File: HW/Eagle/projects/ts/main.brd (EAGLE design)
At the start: 85 x 45 mm, 29 parts, among them IC1 4050D, U1 ATMEGA328P-PU, U2 LM2576T, U3 HT7533

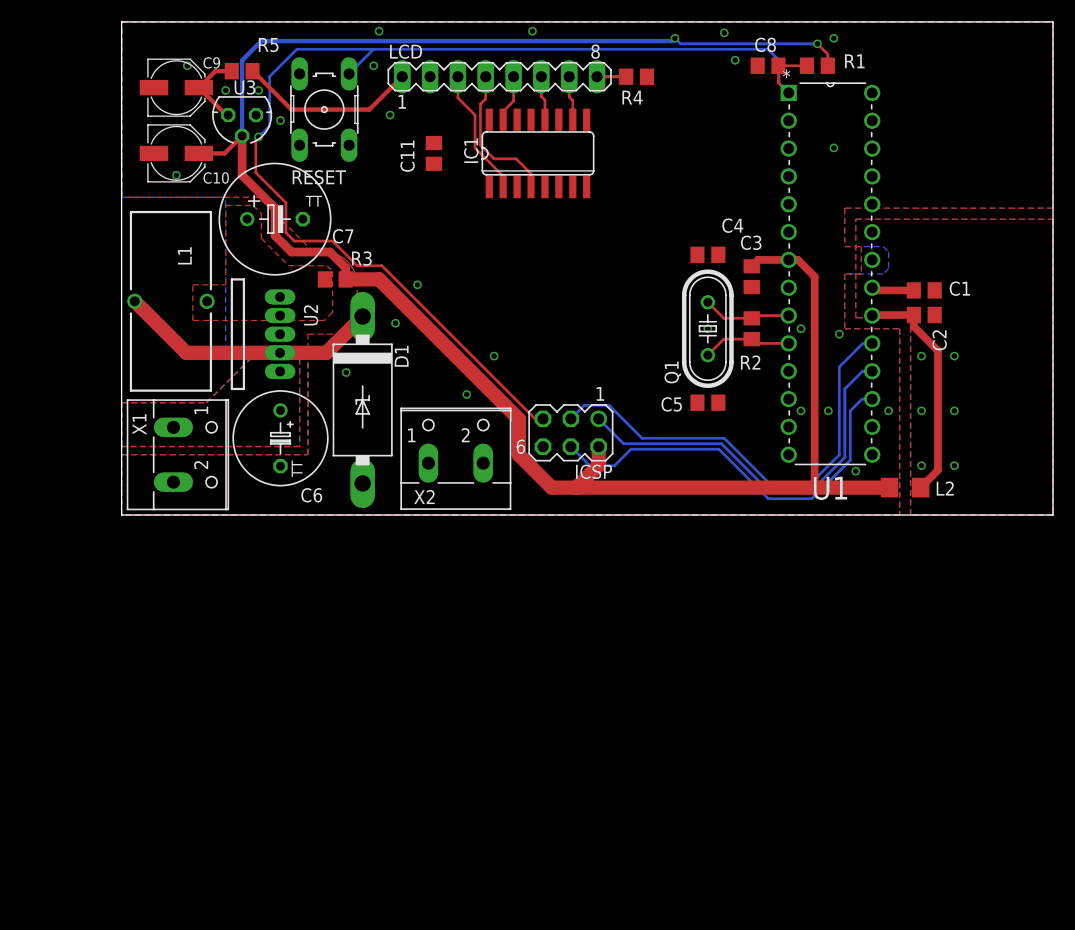
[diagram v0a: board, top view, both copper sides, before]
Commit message: Commit before changing to digital temperature sensor
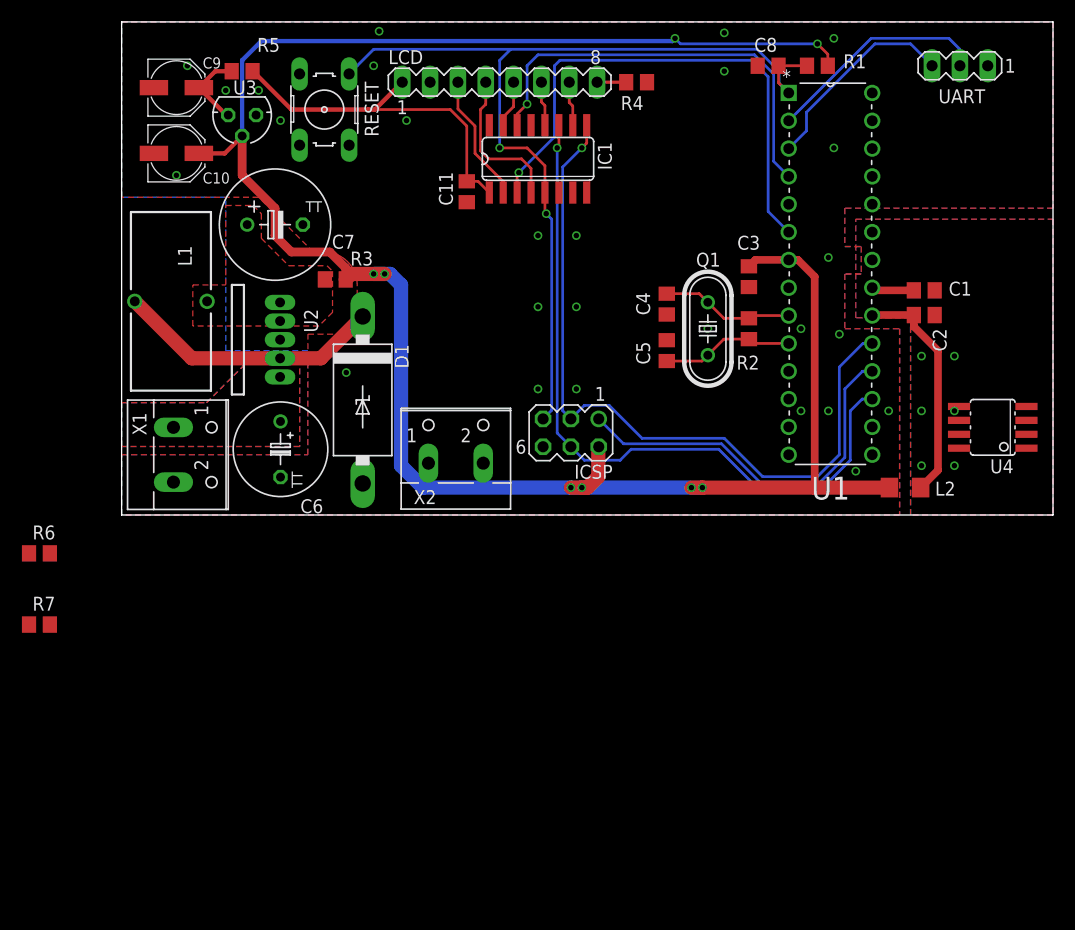
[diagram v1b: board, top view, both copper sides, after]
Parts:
- added R6, R7: 4.7k, rcl:R0805
- added U4: LM75, misc:SOIC8
- added UART: (no value), con-lstb:MA03-1
- moved C5 6.05 mm to (49.8, 15.0), turned to 270 degrees
- moved C4 5.86 mm to (49.8, 19.2), turned to 90 degrees
- moved C11 4.61 mm to (31.5, 29.5), turned to 90 degrees
- moved C6 1.00 mm to (14.5, 6.00)
- moved C7 0.50 mm to (14.0, 26.5)
- moved IC1 0.50 mm to (38.0, 32.5)
- moved LCD 0.50 mm to (34.5, 39.5)
- moved R4 0.50 mm to (47.0, 39.5)
- moved U2 0.50 mm to (12.5, 16.0)
- moved C3 0.25 mm to (57.2, 21.8)
- moved R2 0.25 mm to (57.2, 17.0)
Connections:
- new net LCD_DC_5V: IC1.3, U1.6
- new net LCD_LED_5V: U1.5
- new net LCD_SCE_5V: IC1.14, U1.4
- new net SCL: R6.1, U1.28, U4.2
- new net SDA: R7.1, U1.27, U4.1
- net GND: now also U4.4, UART.1
- net NRST: now also IC1.5
- net RXD: now also UART.2
- net TXD: now also UART.3
- net VCC: now also R6.2, R7.2, U4.8
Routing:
- net LCD_DC_5V: track 0.00 -> 48.3 mm, vias 0 -> 1
- net LCD_SCE_5V: track 0.00 -> 39.4 mm, vias 0 -> 1
- net MOSI: track 37.1 -> 65.8 mm, vias 0 -> 1
- net SCK: track 41.3 -> 68.4 mm, vias 0 -> 1
- net RXD: track 0.00 -> 20.6 mm
- net NRST: track 106.3 -> 86.7 mm, vias 1 -> 2
- net TXD: track 0.00 -> 18.9 mm
- net +3V3: track 16.4 -> 33.3 mm
- net VCC: track 176.4 -> 187.9 mm, vias 2 -> 8
- net N$4: track 8.09 -> 12.1 mm
- net N$3: track 8.15 -> 12.1 mm
- net MISO: track 36.0 -> 35.2 mm
- net LCD_RST: track 13.4 -> 13.9 mm

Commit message: Big Update
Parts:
- removed L2: 10uH, misc:L1206
- added C12: 100nF, rcl:C0805
- added D2, D3: (no value), diode:MINIMELF
- added KEYPAD: (no value), con-lstb:MA07-1
- added LED: (no value), jumper:JP1
- added R10, R11: 10k, rcl:R0805
- added R8: 4.7k, rcl:R0805
- added R9: 330R, rcl:R0805
- added T1, T2: IRLML2502, misc:SOT-23
- moved R6 87.2 mm to (77.0, 18.0), turned to 90 degrees
- moved R7 85.7 mm to (73.5, 18.0), turned to 90 degrees
- moved UART 26.5 mm to (50.5, 36.0), turned to 270 degrees
- moved R4 7.43 mm to (44.5, 32.5), turned to 90 degrees
- moved U4 6.10 mm to (74.5, 11.5)
- moved C4 5.50 mm to (44.2, 19.2)
- moved C5 5.50 mm to (44.2, 15.0)
- moved C8 5.02 mm to (54.0, 41.5)
- moved R1 5.02 mm to (58.5, 41.5)
- moved C1 5.00 mm to (68.2, 20.5)
- moved C2 5.00 mm to (68.2, 18.2)
- moved Q1 5.00 mm to (48.5, 17.0)
- moved U1 5.00 mm to (63.5, 5.50)
- moved C3 4.75 mm to (52.5, 21.8)
- moved R2 4.75 mm to (52.5, 17.0)
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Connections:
- removed net AVCC: C2.2, L2.1, U1.20
- new net KEYPAD_C0: KEYPAD.1, U1.13
- new net KEYPAD_C1: KEYPAD.2, U1.12
- new net KEYPAD_C2: KEYPAD.3, U1.11
- new net KEYPAD_R0: KEYPAD.4, U1.23
- new net KEYPAD_R1: KEYPAD.5, U1.24
- new net KEYPAD_R2: KEYPAD.6, U1.25
- new net KEYPAD_R3: KEYPAD.7, U1.26
- new net LED: LED.2, U1.16
- new net N$10: D2.A, T1.3, X2.1
- new net N$11: D3.A, T2.3, X2.2
- new net N$5: R8.1, U4.5, U4.6, U4.7
- new net N$6: LED.1, R9.2
- new net OUT1: R10.2, T1.1, U1.14
- new net OUT2: R11.2, T2.1, U1.15
- net +12V: now also D2.C, D3.C
- net GND: now also C12.1, R10.1, R11.1, T1.2, T2.2
- net VCC: now also C12.2, C2.2, R8.2, R9.1, U1.20; no longer L2.2
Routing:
- net SDA: track 0.00 -> 50.4 mm
- net SCL: track 0.00 -> 47.7 mm
- net VCC: track 187.9 -> 215.3 mm, vias 8 -> 10
- net KEYPAD_C2: track 0.00 -> 25.5 mm
- net KEYPAD_C0: track 0.00 -> 25.1 mm
- net KEYPAD_C1: track 0.00 -> 24.8 mm
- net AVCC: track 21.1 -> 0.00 mm
- net RXD: track 20.6 -> 5.39 mm
- net LED: track 0.00 -> 15.1 mm
- net TXD: track 18.9 -> 5.39 mm
- net KEYPAD_R2: track 0.00 -> 10.4 mm
- net KEYPAD_R1: track 0.00 -> 10.4 mm
- net KEYPAD_R0: track 0.00 -> 10.1 mm
- net KEYPAD_R3: track 0.00 -> 9.85 mm
- net N$5: track 0.00 -> 5.41 mm
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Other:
- board size 85 x 45 mm -> 80 x 45 mm

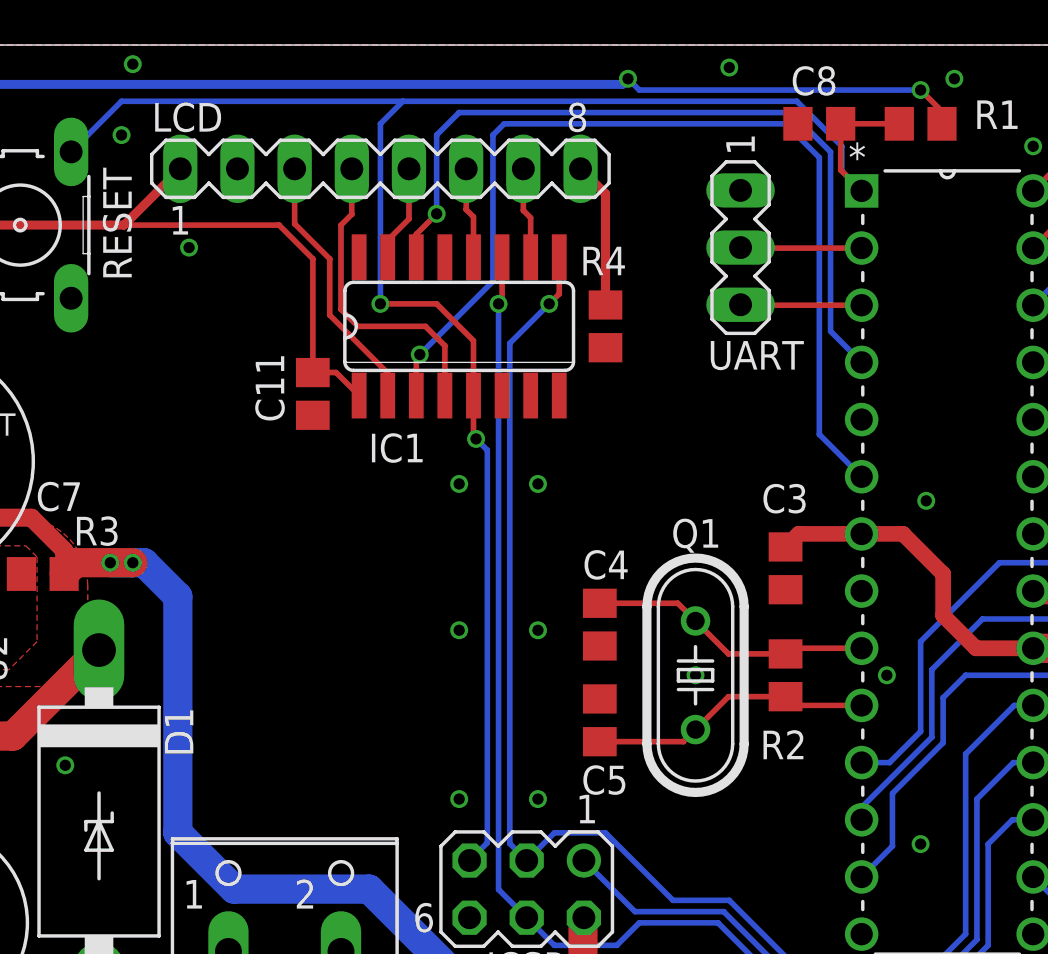
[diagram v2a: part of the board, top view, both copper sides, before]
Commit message: Swaped LCD_SCE_5V and LCD_DC_5V signals on 4050
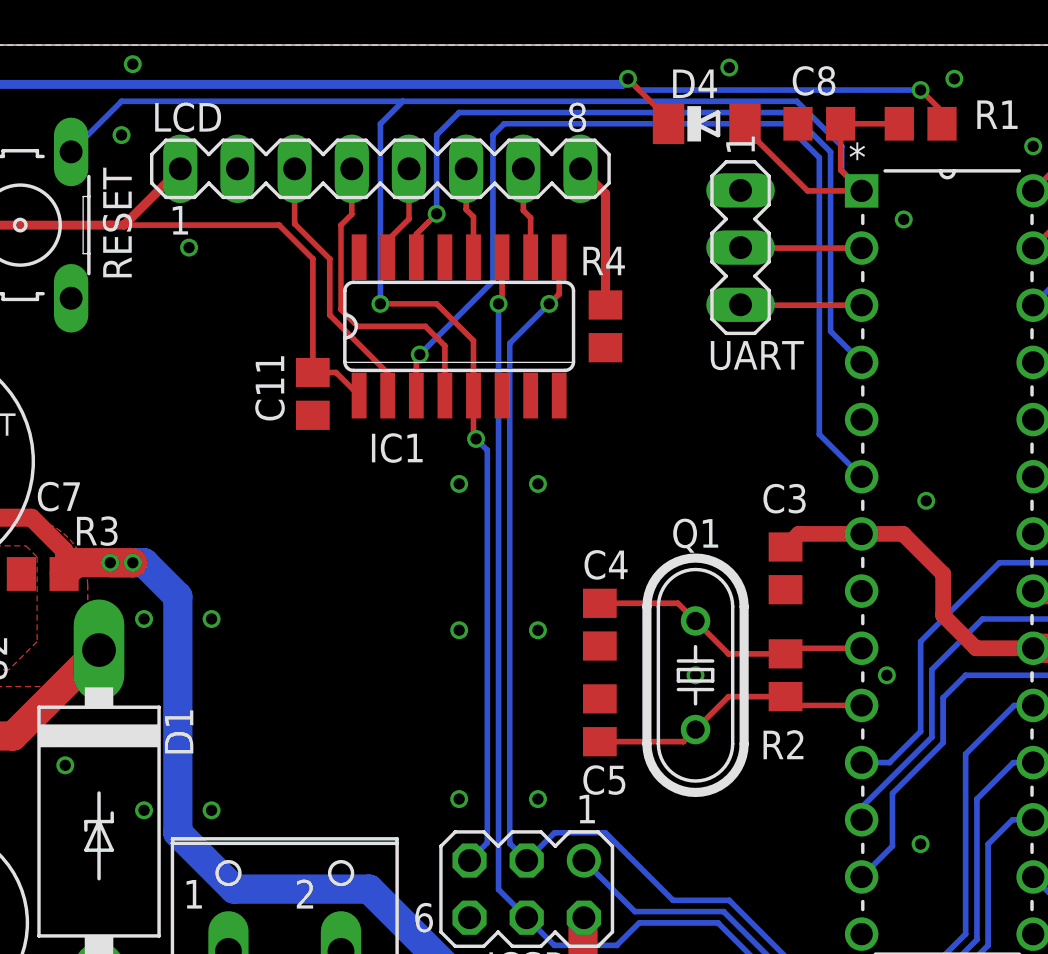
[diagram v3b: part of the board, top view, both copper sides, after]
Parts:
- added D4: (no value), diode:MINIMELF
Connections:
- net LCD_DC_5V: now also IC1.14, U1.4; no longer IC1.3, U1.6
- net LCD_SCE_5V: now also IC1.3, U1.6; no longer IC1.14, U1.4
- net NRST: now also D4.A
- net VCC: now also D4.C
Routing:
- net LCD_SCE_5V: track 34.4 -> 43.3 mm
- net LCD_DC_5V: track 43.3 -> 34.4 mm
- net NRST: track 82.2 -> 88.7 mm
- net VCC: track 215.3 -> 218.0 mm
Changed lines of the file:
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@@
 <element name="D2" library="diode" package="MINIMELF" value="" x="2.5" y="-31"/>
 <element name="D3" library="diode" package="MINIMELF" value="" x="2.5" y="-35"/>
+<element name="D4" library="diode" package="MINIMELF" value="" x="49" y="41.5"/>
 </elements>
 <signals>
@@
 <contactref element="T2" pad="2"/>
 <contactref element="T1" pad="2"/>
+<via x="27" y="19.5" extent="1-16" drill="0.5"/>
+<via x="24" y="19.5" extent="1-16" drill="0.5"/>
+<via x="24" y="11" extent="1-16" drill="0.5"/>
+<via x="27" y="11" extent="1-16" drill="0.5"/>
+<via x="57.75" y="37.25" extent="1-16" drill="0.5"/>
 <wire x1="1.05" y1="-18.5" x2="1.05" y2="-25" width="0" layer="19" extent="1-1"/>
 <wire x1="3.45" y1="-12.6" x2="1.05" y2="-18.5" width="0" layer="19" extent="1-1"/>
@@
 <wire x1="34" y1="7.5" x2="39" y2="2.5" width="1.3" layer="16"/>
 <wire x1="39" y1="2.5" x2="41" y2="2.5" width="1.3" layer="16"/>
+<contactref element="D4" pad="C"/>
+<wire x1="47.3" y1="41.5" x2="47.3" y2="41.7" width="0.4064" layer="1"/>
+<wire x1="47.3" y1="41.7" x2="45.5" y2="43.5" width="0.25" layer="1"/>
 </signal>
 <signal name="AREF">
@@
 <wire x1="38.635" y1="27.615" x2="38.635" y2="29.4266" width="0.25" layer="1"/>
 <wire x1="34.5" y1="41.5" x2="35.5" y2="42.5" width="0.25" layer="16"/>
+<contactref element="D4" pad="A"/>
+<wire x1="50.7" y1="41.5" x2="50.7" y2="41.3" width="0.25" layer="1"/>
+<wire x1="50.7" y1="41.3" x2="53.48" y2="38.52" width="0.25" layer="1"/>
+<wire x1="53.48" y1="38.52" x2="55.88" y2="38.52" width="0.25" layer="1"/>
 </signal>
 <signal name="N$7">
@@
 </signal>
 <signal name="LCD_SCE_5V">
-<contactref element="U1" pad="4"/>
-<contactref element="IC1" pad="14"/>
-<wire x1="36.095" y1="35.5734" x2="36.095" y2="36.595" width="0.25" layer="1"/>
-<wire x1="36.095" y1="36.595" x2="37" y2="37.5" width="0.25" layer="1"/>
-<via x="37" y="37.5" extent="1-16" drill="0.5"/>
-<wire x1="37" y1="37.5" x2="37" y2="41" width="0.25" layer="16"/>
-<wire x1="37" y1="41" x2="38" y2="42" width="0.25" layer="16"/>
-<wire x1="38" y1="42" x2="52.75" y2="42" width="0.25" layer="16"/>
-<wire x1="52.75" y1="42" x2="54.5" y2="40.25" width="0.25" layer="16"/>
-<wire x1="54.5" y1="40.25" x2="54.5" y2="32.28" width="0.25" layer="16"/>
-<wire x1="54.5" y1="32.28" x2="55.88" y2="30.9" width="0.25" layer="16"/>
-</signal>
-<signal name="LCD_DC_5V">
 <contactref element="U1" pad="6"/>
 <contactref element="IC1" pad="3"/>
@@
 <wire x1="54" y1="27.7" x2="55.88" y2="25.82" width="0.25" layer="16"/>
 </signal>
+<signal name="LCD_DC_5V">
+<contactref element="U1" pad="4"/>
+<contactref element="IC1" pad="14"/>
+<wire x1="36.095" y1="35.5734" x2="36.095" y2="36.595" width="0.25" layer="1"/>
+<wire x1="36.095" y1="36.595" x2="37" y2="37.5" width="0.25" layer="1"/>
+<via x="37" y="37.5" extent="1-16" drill="0.5"/>
+<wire x1="37" y1="37.5" x2="37" y2="41" width="0.25" layer="16"/>
+<wire x1="37" y1="41" x2="38" y2="42" width="0.25" layer="16"/>
+<wire x1="38" y1="42" x2="52.75" y2="42" width="0.25" layer="16"/>
+<wire x1="52.75" y1="42" x2="54.5" y2="40.25" width="0.25" layer="16"/>
+<wire x1="54.5" y1="40.25" x2="54.5" y2="32.28" width="0.25" layer="16"/>
+<wire x1="54.5" y1="32.28" x2="55.88" y2="30.9" width="0.25" layer="16"/>
+</signal>
 <signal name="LCD_LED_5V">

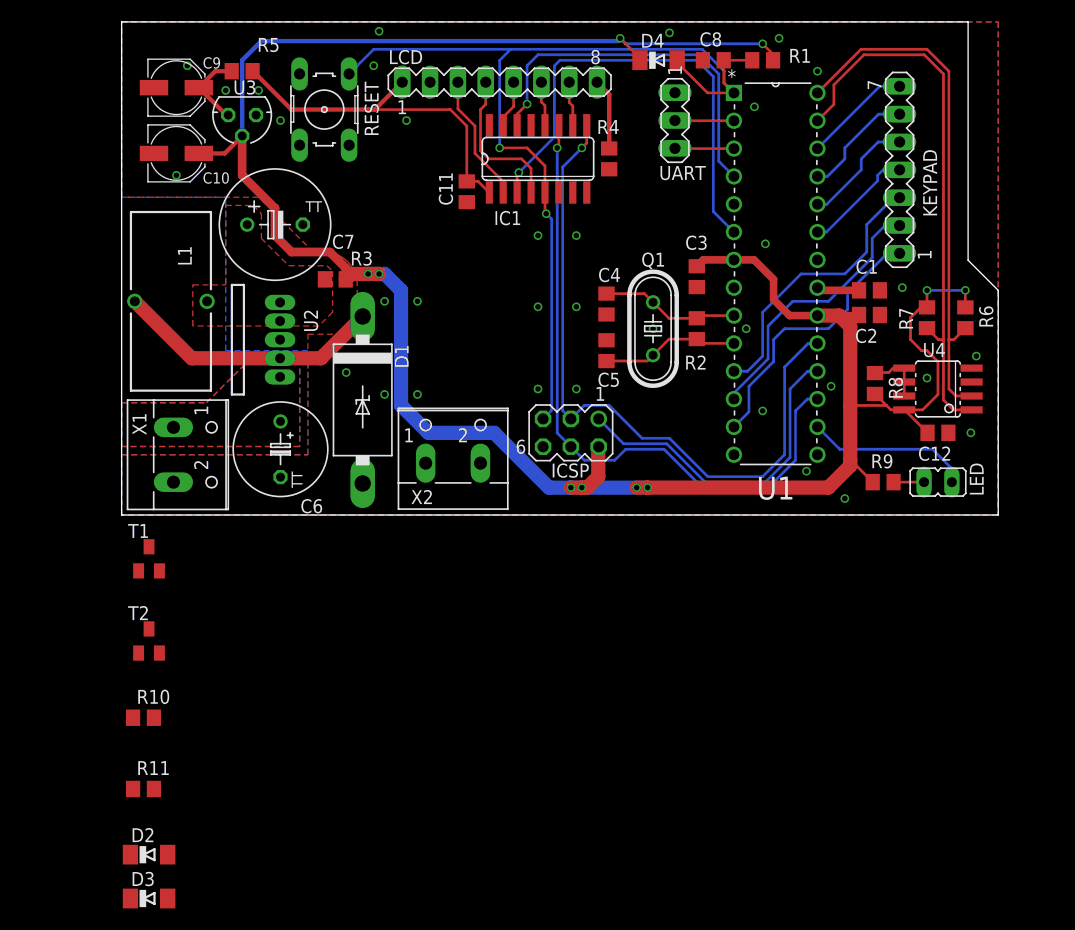
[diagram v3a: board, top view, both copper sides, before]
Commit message: Added Power CMOS transistors
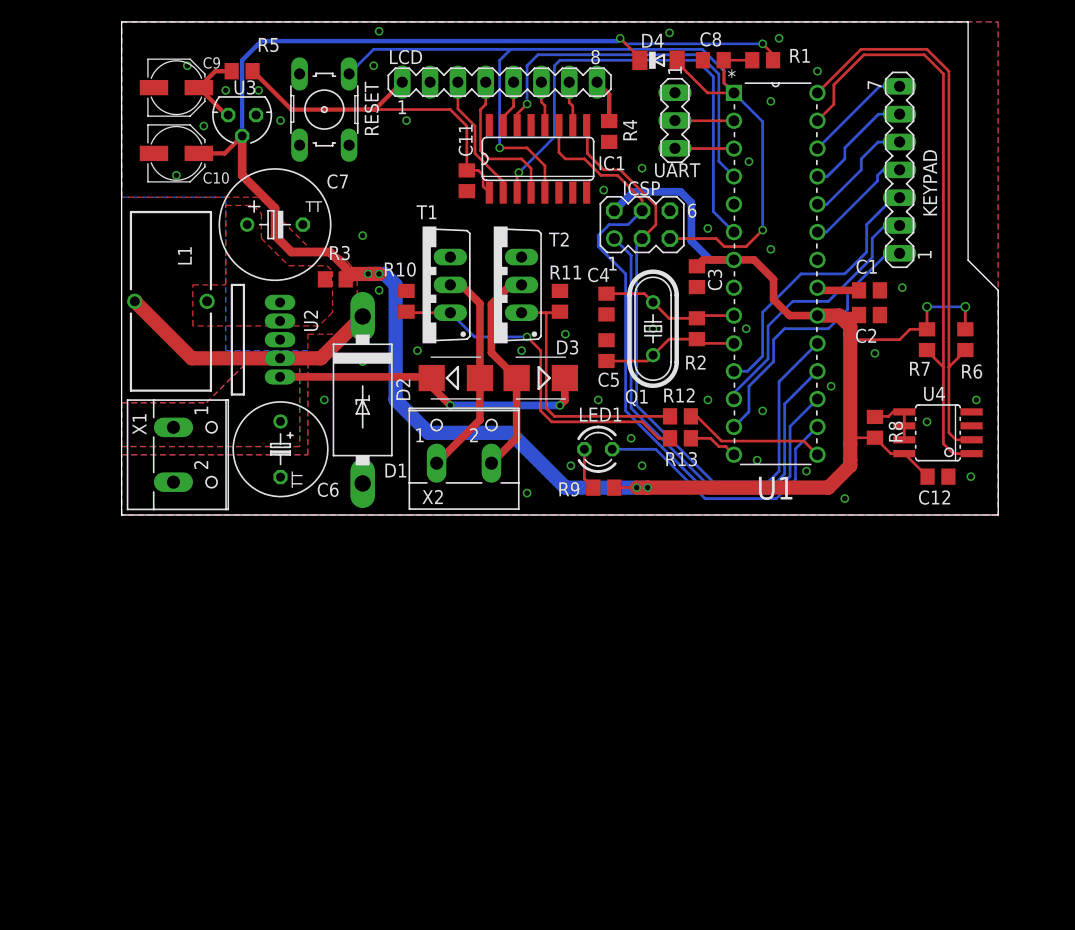
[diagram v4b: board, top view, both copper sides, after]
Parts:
- removed LED: (no value), jumper:JP1
- added LED1: (no value), led:LED3MM
- added R12, R13: 330R, rcl:R0805
- D2, D3: value (none) -> SS210; device diode:MINIMELF -> diode:SMB
- T1, T2: value IRLML2502 -> IRFZ24N; device misc:SOT-23 -> misc:TO220AB
- moved D3 59.5 mm to (38.2, 12.5), turned to 180 degrees
- moved R11 58.5 mm to (40.0, 19.5), turned to 270 degrees
- moved D2 51.7 mm to (30.5, 12.5)
- moved T2 47.0 mm to (36.5, 21.0), turned to 90 degrees
- moved R10 44.9 mm to (26.0, 19.5), turned to 270 degrees
- moved T1 37.2 mm to (30.0, 21.0), turned to 90 degrees
- moved R9 25.5 mm to (44.0, 2.50), turned to 180 degrees
- moved ICSP 20.1 mm to (47.5, 26.5), turned to 0 degrees
- moved C12 4.00 mm to (74.5, 3.50)
- moved R8 4.00 mm to (68.8, 8.00)
- moved U4 4.00 mm to (74.5, 7.50)
- moved R4 2.50 mm to (44.5, 35.0)
- moved R6 2.00 mm to (77.0, 16.0)
- moved R7 2.00 mm to (73.5, 16.0)
- moved C11 1.00 mm to (31.5, 30.5)
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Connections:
- new net N$12: R11.2, R12.1, T2.G
- new net N$9: R10.2, R13.1, T1.G
- net GND: now also T1.S, T2.S; no longer T1.2, T2.2
- net LED: now also LED1.K; no longer LED.2
- net N$10: now also T1.D; no longer T1.3
- net N$11: now also T2.D; no longer T2.3
- net N$6: now also LED1.A; no longer LED.1
- net OUT1: now also R13.2; no longer R10.2, T1.1
- net OUT2: now also R12.2; no longer R11.2, T2.1
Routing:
- net N$9: track 0.00 -> 34.6 mm, vias 0 -> 1
- net +12V: track 0.00 -> 29.8 mm, vias 0 -> 2
- net N$12: track 0.00 -> 23.9 mm
- net N$11: track 0.00 -> 19.9 mm
- net N$10: track 0.00 -> 19.6 mm
- net MISO: track 30.2 -> 44.3 mm
- net OUT2: track 0.00 -> 13.0 mm
- net LED: track 15.1 -> 24.9 mm
- net OUT1: track 0.00 -> 4.55 mm
- net SDA: track 50.4 -> 54.6 mm
- net SCL: track 47.7 -> 52.0 mm
- net SCK: track 63.4 -> 59.2 mm, vias 1 -> 0
- net VCC: track 218.0 -> 221.7 mm, vias 10 -> 8
- net LCD_LED: track 6.51 -> 4.01 mm
- net NRST: track 88.7 -> 90.5 mm
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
